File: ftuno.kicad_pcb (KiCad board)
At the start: 2 copper layers, 68.6 x 53.3 mm, 70 parts, among them CN1 AFC10-S04QCA-00, J1 Conn_01x08_Pin, J10 Conn_02x04_Odd_Even, J11 Conn_01x04_Socket, J2 Conn_01x08_Socket, J3 Conn_01x06_Pin, J4 Conn_01x06_Socket, J5 Conn_01x10_Pin, J6 Conn_01x10_Socket, J7 Conn_01x08_Pin, J8 Conn_01x08_Socket, J9 Conn_02x03_Odd_Even, Q1 AO3401, Q2 BSS138PS_C5224289, Q3 BSS138PS_C5224289, SW1 SK12D07VG4, SW2 TS-1187A-B-A-B, U1 ATmega328P-A, U2 CH340C, U3 SRV05-4, U4 TPS54302, U5 ME6217C33M5G, X1 CSTCE16M0V53-R0

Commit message: use more common DC conn
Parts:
- DC1: value DC-005 5.5-2.0MM -> DC-005-20A; footprint uno:DC-IN-TH_DC-5520-1 -> uno:DC-IN-TH_DC-005-20A
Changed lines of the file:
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@@
       (plot_on_all_layers_selection 0x0000000_00000000)
       (disableapertmacros false)
-      (usegerberextensions false)
+      (usegerberextensions true)
       (usegerberattributes true)
       (usegerberadvancedattributes true)
@@
       (outputformat 1)
       (mirror false)
-      (drillshape 1)
+      (drillshape 0)
       (scaleselection 1)
       (outputdirectory "")
@@
       (net 43 "RX0") (pinfunction "Pin_8") (pintype "passive"))
   )
-  (footprint "uno:DC-IN-TH_DC-5520-1" (layer "F.Cu")
+  (footprint "uno:DC-IN-TH_DC-005-20A" (layer "F.Cu")
     (at 78.643 86.6825)
-    (property "LCSC Part" "C16214")
+    (property "LCSC Part" "C136744")
     (property "Sheetfile" "ftuno.kicad_sch")
     (property "Sheetname" "")
@@
     (property "ki_keywords" "DC power barrel jack connector")
     (attr through_hole)
-    (fp_text reference "DC1" (at -0.0046 -2.3037) (layer "F.SilkS")
-        (effects (font (size 0.6 0.6) (thickness 0.08)))
-    )
-    (fp_text value "DC-005 5.5-2.0MM" (at 0 6.4) (layer "F.Fab")
+    (fp_text reference "DC1" (at 0 -2.3545) (layer "F.SilkS")
+        (effects (font (size 1 1) (thickness 0.15)))
+    )
+    (fp_text value "DC-005-20A " (at 0 6.32) (layer "F.Fab")
         (effects (font (size 1 1) (thickness 0.15)))
     )
@@
         (effects (font (size 1 1) (thickness 0.15)))
     )
-    (fp_line (start -10.5 -6.86) (end 3.7 -6.86)
-      (stroke (width 0.25) (type solid)) (layer "F.SilkS"))
-    (fp_line (start -10.5 -6.85) (end -10.5 2.14)
-      (stroke (width 0.25) (type solid)) (layer "F.SilkS"))
-    (fp_line (start -10.5 2.14) (end -2.33 2.14)
-      (stroke (width 0.25) (type solid)) (layer "F.SilkS"))
-    (fp_line (start -7.74 -6.85) (end -7.74 2.15)
-      (stroke (width 0.25) (type solid)) (layer "F.SilkS"))
-    (fp_line (start -1.7 2.14) (end -2.33 2.14)
-      (stroke (width 0.25) (type solid)) (layer "F.SilkS"))
-    (fp_line (start 3.7 -6.86) (end 3.7 -4.39)
-      (stroke (width 0.25) (type solid)) (layer "F.SilkS"))
-    (fp_line (start 3.7 -0.41) (end 3.7 2.14)
-      (stroke (width 0.25) (type solid)) (layer "F.SilkS"))
-    (fp_line (start 3.7 2.14) (end 2.7 2.14)
-      (stroke (width 0.25) (type solid)) (layer "F.SilkS"))
-    (fp_circle (center 3.7 2.6) (end 3.73 2.6)
+    (fp_line (start -10.51 -6.77) (end 3.71 -6.77)
+      (stroke (width 0.25) (type solid)) (layer "F.SilkS"))
+    (fp_line (start -10.51 2.23) (end -10.51 -6.77)
+      (stroke (width 0.25) (type solid)) (layer "F.SilkS"))
+    (fp_line (start -10.51 2.23) (end -1.47 2.24)
+      (stroke (width 0.25) (type solid)) (layer "F.SilkS"))
+    (fp_line (start -7.4 2.22) (end -7.4 -6.78)
+      (stroke (width 0.25) (type solid)) (layer "F.SilkS"))
+    (fp_line (start -7.32 -5.48) (end 3.71 -5.47)
+      (stroke (width 0.25) (type solid)) (layer "F.SilkS"))
+    (fp_line (start -7.32 0.92) (end 3.7 0.92)
+      (stroke (width 0.25) (type solid)) (layer "F.SilkS"))
+    (fp_line (start 2.47 2.22) (end 3.7 2.22)
+      (stroke (width 0.25) (type solid)) (layer "F.SilkS"))
+    (fp_line (start 3.7 -6.78) (end 3.7 -4.27)
+      (stroke (width 0.25) (type solid)) (layer "F.SilkS"))
+    (fp_line (start 3.7 -0.28) (end 3.7 2.22)
+      (stroke (width 0.25) (type solid)) (layer "F.SilkS"))
+    (fp_circle (center 3.47 -4.01) (end 3.72 -4.01)
+      (stroke (width 0.5) (type solid)) (fill none) (layer "Cmts.User"))
+    (fp_circle (center 3.7 -6.78) (end 3.73 -6.78)
       (stroke (width 0.06) (type solid)) (fill none) (layer "F.Fab"))
-    (pad "1" thru_hole oval (at 3 -2.4 90) (size 4 1.3) (drill oval 3.499993 0.799998) (layers "*.Cu" "*.Mask")
+    (pad "1" thru_hole oval (at 3 -2.32) (size 1.5 3.8) (drill oval 0.900024 3.100172) (layers "*.Cu" "*.Mask")
       (net 19 "Net-(D1-A)") (pintype "passive"))
-    (pad "2" thru_hole oval (at 0.5 2.4) (size 4 1.3) (drill oval 3.499993 0.799998) (layers "*.Cu" "*.Mask")
+    (pad "2" thru_hole oval (at -3 -2.32 180) (size 1.5 3.8) (drill oval 0.900024 3.100172) (layers "*.Cu" "*.Mask")
       (net 1 "GND") (pintype "passive"))
-    (pad "3" thru_hole oval (at -3 -2.4 270) (size 4 1.3) (drill oval 3.499993 0.799998) (layers "*.Cu" "*.Mask")
+    (pad "3" thru_hole oval (at 0.5 2.32 270) (size 1.5 3.4) (drill oval 0.900024 2.599792) (layers "*.Cu" "*.Mask")
       (net 1 "GND") (pintype "passive"))
-    (model "C:/Users/wb/Documents/electronics/ftuno/lib/uno.3dshapes/DC-IN-TH_DC-5520-1.wrl"
-      (offset (xyz -3.5 2.15 0))
+    (model "C:/Users/wb/Documents/electronics/ftuno/lib/uno.3dshapes/DC-IN-TH_DC-005-20A.wrl"
+      (offset (xyz -3.45 2.12 0))
       (scale (xyz 1 1 1))
       (rotate (xyz 0 0 90))

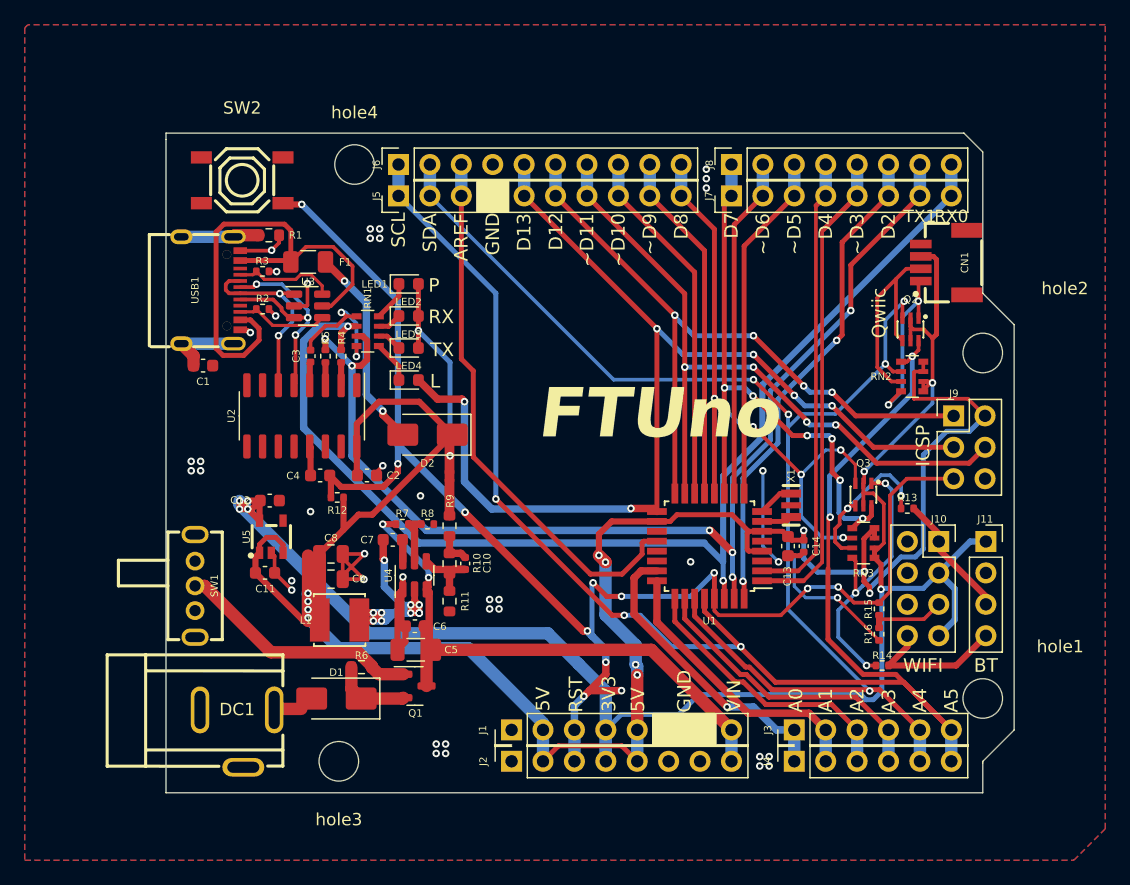
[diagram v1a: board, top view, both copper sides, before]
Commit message: PCB update, replace USB conn, replace TVS, cleanup
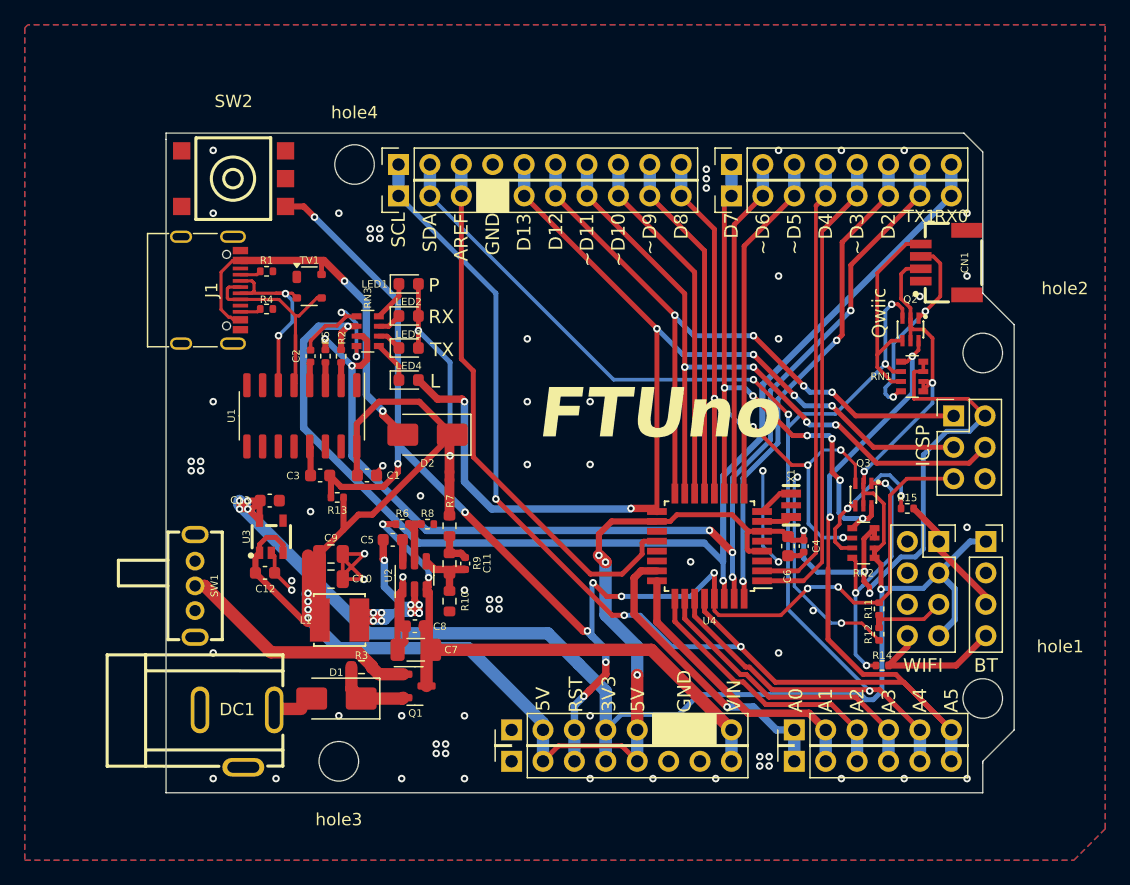
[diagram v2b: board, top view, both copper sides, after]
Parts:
- removed the C1 at (75.9, 56.5)
- removed F1: 0466002.NRHF, Fuse:Fuse_1206_3216Metric
- removed the R2 at (80.7, 51.9)
- removed the R3 at (80.7, 48.9)
- removed the U3 at (84.4, 51.7)
- removed USB1: TYPE-C 16PIN 2MD(073), uno:USB-C-SMD_TYPE-C-6PIN-2MD-073
- added J1: USB_C_Receptacle_USB2.0_16P, Connector_USB:USB_C_Receptacle_G-Switch_GT-USB-7010ASV, F.Cu at (75.2, 50.4)
- added R4: 5.1k, Resistor_SMD:R_0402_1005Metric, F.Cu at (81.0, 51.9)
- added TV1: PRTR5V0U2X, Package_TO_SOT_SMD:SOT-143, F.Cu at (84.5, 50.1)
- R1: value 1M -> 5.1k; footprint Resistor_SMD:R_0603_1608Metric -> Resistor_SMD:R_0402_1005Metric
- SW2: value TS-1187A-B-A-B -> SKHMQLE010; footprint uno:SW-SMD_4P-L5.1-W5.1-P3.70-LS6.5-TL-2 -> uno:KEY-SMD_4P-L6.2-W6.5-P4.50-LS8.0_SKHMXX
- moved R1 2.92 mm to (81.0, 48.9), turned to 0 degrees
- moved SW2 0.71 mm to (78.4, 41.4)
- renumbered C2 to C1, C9 to C10, C10 to C11, C11 to C12, C12 to C13, C3 to C2, C4 to C3, C14 to C4, C7 to C5, C13 to C6, C5 to C7, C6 to C8, C8 to C9, J6 to J10, J7 to J11, J8 to J12, J9 to J2, J1 to J3, J2 to J4, J10 to J5, J3 to J6, J4 to J7, J11 to J8, J5 to J9, R11 to R10, R15 to R11, R16 to R12, R12 to R13, R13 to R15, R4 to R2, R6 to R3, R7 to R6, R9 to R7, R10 to R9, RN2 to RN1, RN3 to RN2, RN1 to RN3, U2 to U1, U4 to U2, U5 to U3, U1 to U4
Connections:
- CN1 pad 1: SCL -> GND
- CN1 pad 2: SDA -> +3.3V
- CN1 pad 3: +3.3V -> SCL
- CN1 pad 4: GND -> SDA
- CN1 pad 5: unconnected-(CN1-Pad5) -> GND
- CN1 pad 6: unconnected-(CN1-Pad6) -> GND
- R1 pad 1: GND -> Net-(J1-CC1)
- R1 pad 2: Net-(R1-Pad2) -> GND
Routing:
- net Net-(U3-VP): track 40.4 -> 0.00 mm
- net VBUS: track 16.8 -> 31.8 mm
- net CC1: track 8.22 -> 0.00 mm
- net CC2: track 7.53 -> 0.00 mm
- net Net-(C1-Pad2): track 6.39 -> 0.00 mm
- net Net-(R1-Pad2): track 6.31 -> 0.00 mm
- net RESET: track 119.2 -> 115.5 mm, vias 12 -> 11
- net DP: track 19.2 -> 16.3 mm, vias 3 -> 0
- net SCL: track 14.0 -> 16.5 mm
- net GND: track 67.8 -> 65.3 mm, vias 42 -> 74
- net +3.3V: track 144.4 -> 142.2 mm
- net Net-(J1-CC1): track 0.00 -> 1.72 mm
- net Net-(J1-CC2): track 0.00 -> 1.70 mm
- net Net-(Q3-S1): track 22.5 -> 21.4 mm
- net DN: track 15.7 -> 16.6 mm
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
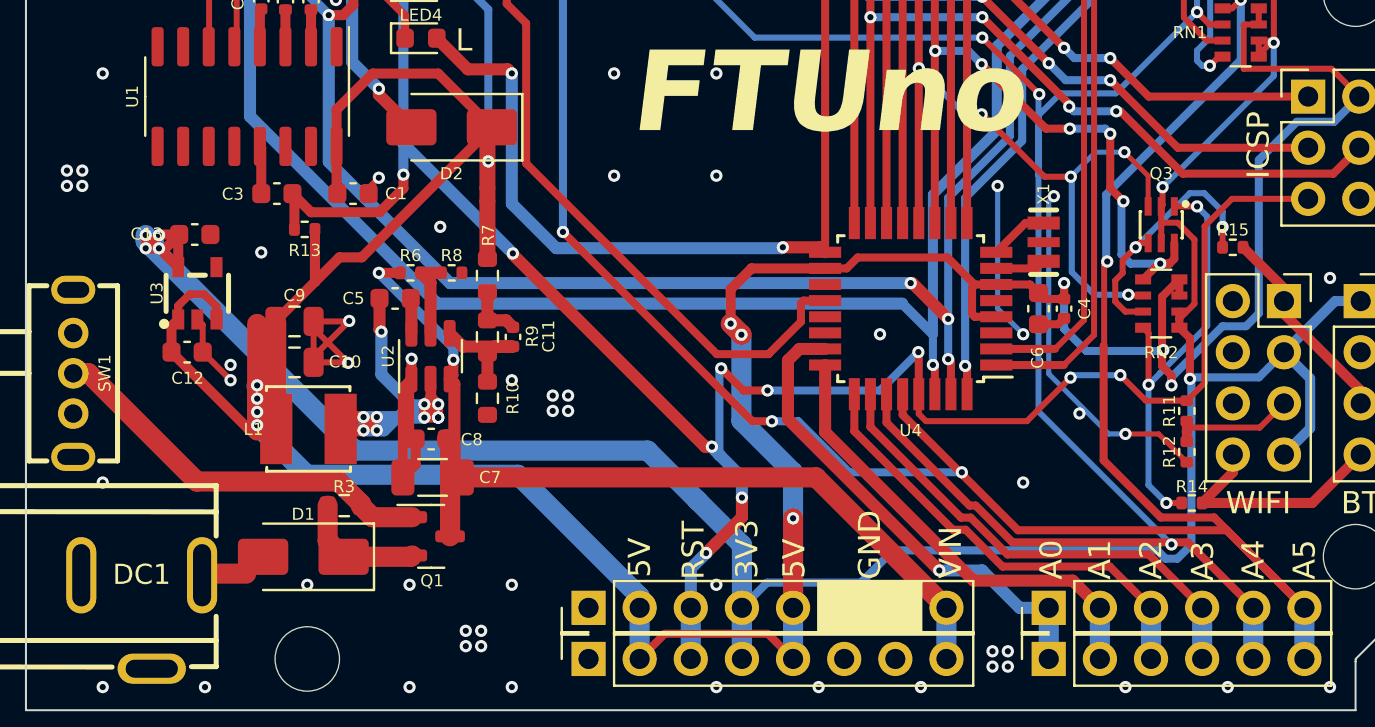
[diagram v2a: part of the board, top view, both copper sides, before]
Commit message: get rid of buck convertor and use LDO instead
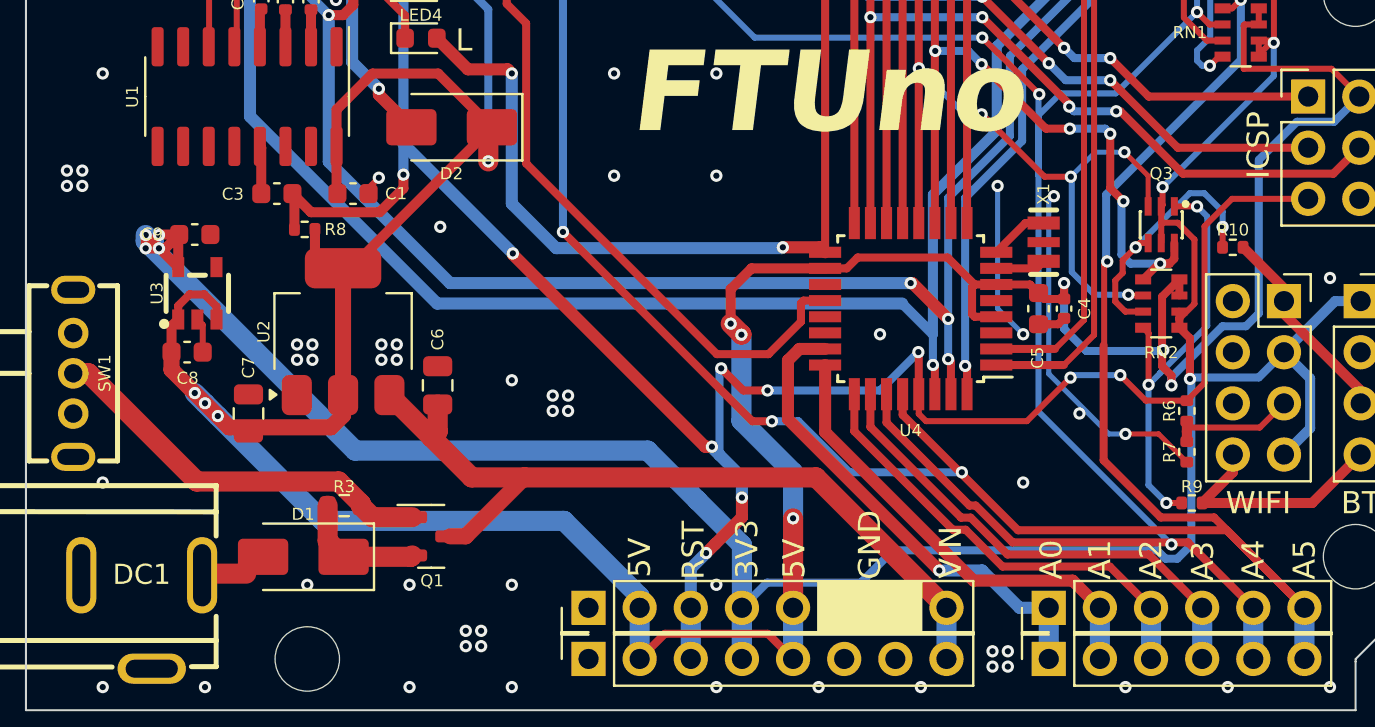
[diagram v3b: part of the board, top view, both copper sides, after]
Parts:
- removed C10: 22u, Capacitor_SMD:C_0805_2012Metric
- removed C11: 75p, Capacitor_SMD:C_0402_1005Metric
- removed the C5 at (91.2, 70.6)
- removed the C8 at (93.0, 77.6)
- removed the C9 at (86.2, 71.8)
- removed L1: SWPA4030S100MT, uno:IND-SMD_L4.0-W4.0
- removed the R10 at (95.8, 75.6)
- removed the R6 at (92.0, 69.3)
- removed the R7 at (95.8, 69.5)
- removed the R8 at (94.0, 69.3)
- removed the R9 at (95.8, 72.5)
- added C6: 22u, Capacitor_SMD:C_0805_2012Metric, F.Cu at (93.3, 74.9)
- C7: value 10u -> 22u; footprint Capacitor_SMD:C_1206_3216Metric -> Capacitor_SMD:C_0805_2012Metric
- U2: value TPS54302 -> SPX1117M3-L-5-0; footprint Package_TO_SOT_SMD:SOT-23-6 -> Package_TO_SOT_SMD:SOT-223-3_TabPin2
- moved C7 9.68 mm to (83.9, 76.3), turned to 90 degrees
- moved U2 4.51 mm to (88.6, 72.3)
- renumbered C6 to C5, C12 to C8, C13 to C9, R15 to R10, R11 to R6, R12 to R7, R13 to R8, R14 to R9
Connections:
- C7 pad 1: VDC -> +5V
- U2 pad 2: Net-(U2-SW) -> +5V
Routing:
- net Net-(U2-SW): track 26.9 -> 0.00 mm, vias 10 -> 0
- net GND: track 65.3 -> 40.8 mm, vias 74 -> 76
- net +5V: track 198.8 -> 192.4 mm, vias 12 -> 11
- net Net-(U2-FB): track 6.23 -> 0.00 mm
- net VDC: track 47.4 -> 41.3 mm, vias 2 -> 0
- net Net-(U2-EN): track 4.22 -> 0.00 mm
- net Net-(C11-Pad1): track 2.81 -> 0.00 mm
- net Net-(U2-BOOT): track 1.75 -> 0.00 mm

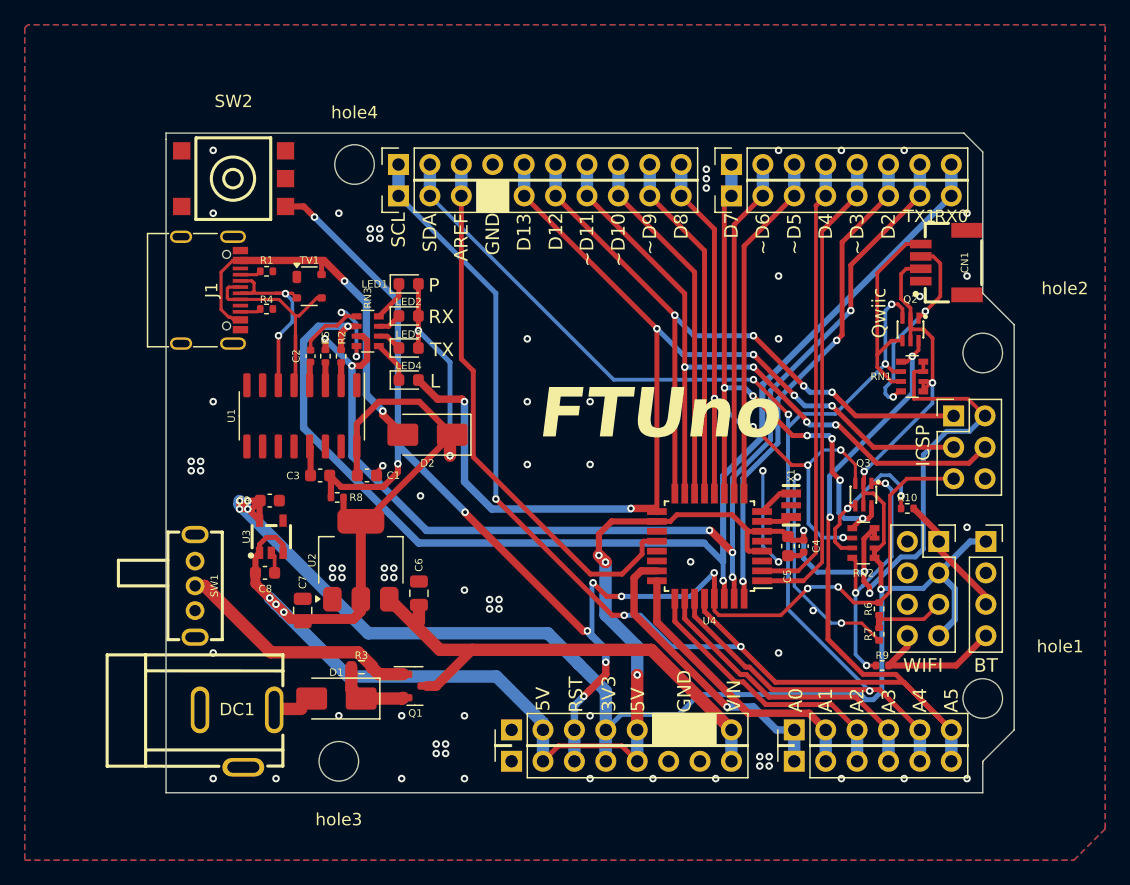
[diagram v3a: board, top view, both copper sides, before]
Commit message: fix qwiic pin arrangement, move usb conn
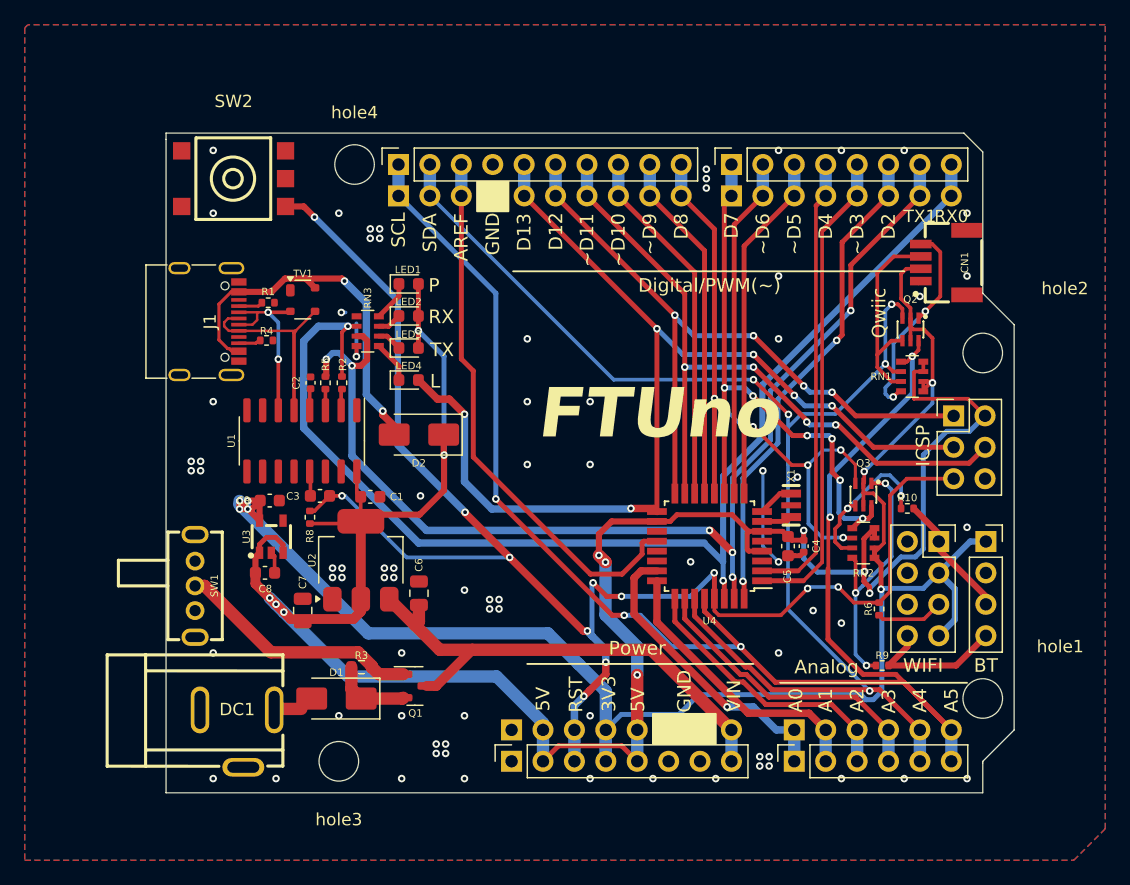
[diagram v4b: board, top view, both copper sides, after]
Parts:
- removed R7: 2k, Resistor_SMD:R_0402_1005Metric
- R6: value 1k -> 2.2k
- moved R8 2.73 mm to (84.5, 68.8), turned to -90 degrees
- moved J1 2.54 mm to (75.1, 53.0)
- moved R1 2.54 mm to (81.2, 51.4)
- moved R4 2.54 mm to (81.0, 54.5)
- moved C2 2.16 mm to (84.6, 57.9)
- moved R2 2.15 mm to (87.1, 57.9)
- moved R5 2.15 mm to (85.8, 57.9)
- moved U1 2.03 mm to (83.9, 62.6)
- moved C1 1.75 mm to (89.4, 67.1)
- moved C3 1.65 mm to (85.3, 67.1)
- moved TV1 1.20 mm to (83.9, 51.2)
- moved D2 0.69 mm to (93.3, 62.1)
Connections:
- CN1 pad 3: SCL -> SDA
- CN1 pad 4: SDA -> SCL
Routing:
- net GND: track 40.8 -> 15.6 mm
- net +5V: track 192.4 -> 184.0 mm
- net RESET: track 115.5 -> 123.8 mm, vias 11 -> 12
- net RX0: track 95.2 -> 97.3 mm
- net DN: track 16.6 -> 14.7 mm
- net SWRST: track 6.42 -> 5.45 mm
- net D13/SCK: track 88.0 -> 87.4 mm
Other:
- board text added: "Analog"
- board text added: "Digital/PWM(~)"
- board text added: "Power"

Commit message: refine 1117 in and out
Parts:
- removed DC1: DC-005-20A, uno:DC-IN-TH_DC-005-20A
- removed R6: 2.2k, Resistor_SMD:R_0402_1005Metric
- added C10: 47u, Capacitor_SMD:CP_Elec_6.3x5.4, F.Cu at (95.5, 81.7)
- added C11: 47u, Capacitor_SMD:CP_Elec_6.3x5.4, F.Cu at (88.4, 81.7)
- added J13: DC050-T, uno:DC-IN_DC050-T, F.Cu at (77.4, 83.6)
- C6, C7: value 22u -> 100n; footprint Capacitor_SMD:C_0805_2012Metric -> Capacitor_SMD:C_0603_1608Metric
- moved D1 14.1 mm to (98.0, 75.1)
- moved R3 12.7 mm to (97.8, 72.0)
- moved Q1 11.5 mm to (94.5, 71.0), turned to 90 degrees
- moved SW1 3.56 mm to (75.2, 70.8)
- moved C7 0.27 mm to (84.1, 76.1)
- moved C6 0.18 mm to (93.2, 74.8)
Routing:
- net Net-(D1-A): track 3.38 -> 44.3 mm, vias 0 -> 4
- net Net-(Q1-G): track 19.9 -> 33.0 mm, vias 0 -> 1
- net GND: track 15.6 -> 22.2 mm, vias 76 -> 33
- net SWRST: track 5.45 -> 0.00 mm
- net +5V: track 184.0 -> 185.9 mm
- net VDC: track 41.3 -> 42.9 mm
